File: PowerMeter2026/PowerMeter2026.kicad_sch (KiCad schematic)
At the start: 44 parts, among them J1 STRAIN, J5 USB_C_Receptacle_USB2.0_14P, Q3 MMBT3904, Q4 MMBT3904, SW4 CELL, SW5 RST, SW6 BOOT, U1 ESP32-WROOM-32, U11 HT7733, U5 HX711, U8 LM1117MP-3.3, U9 CH340G, Y2 12MHz

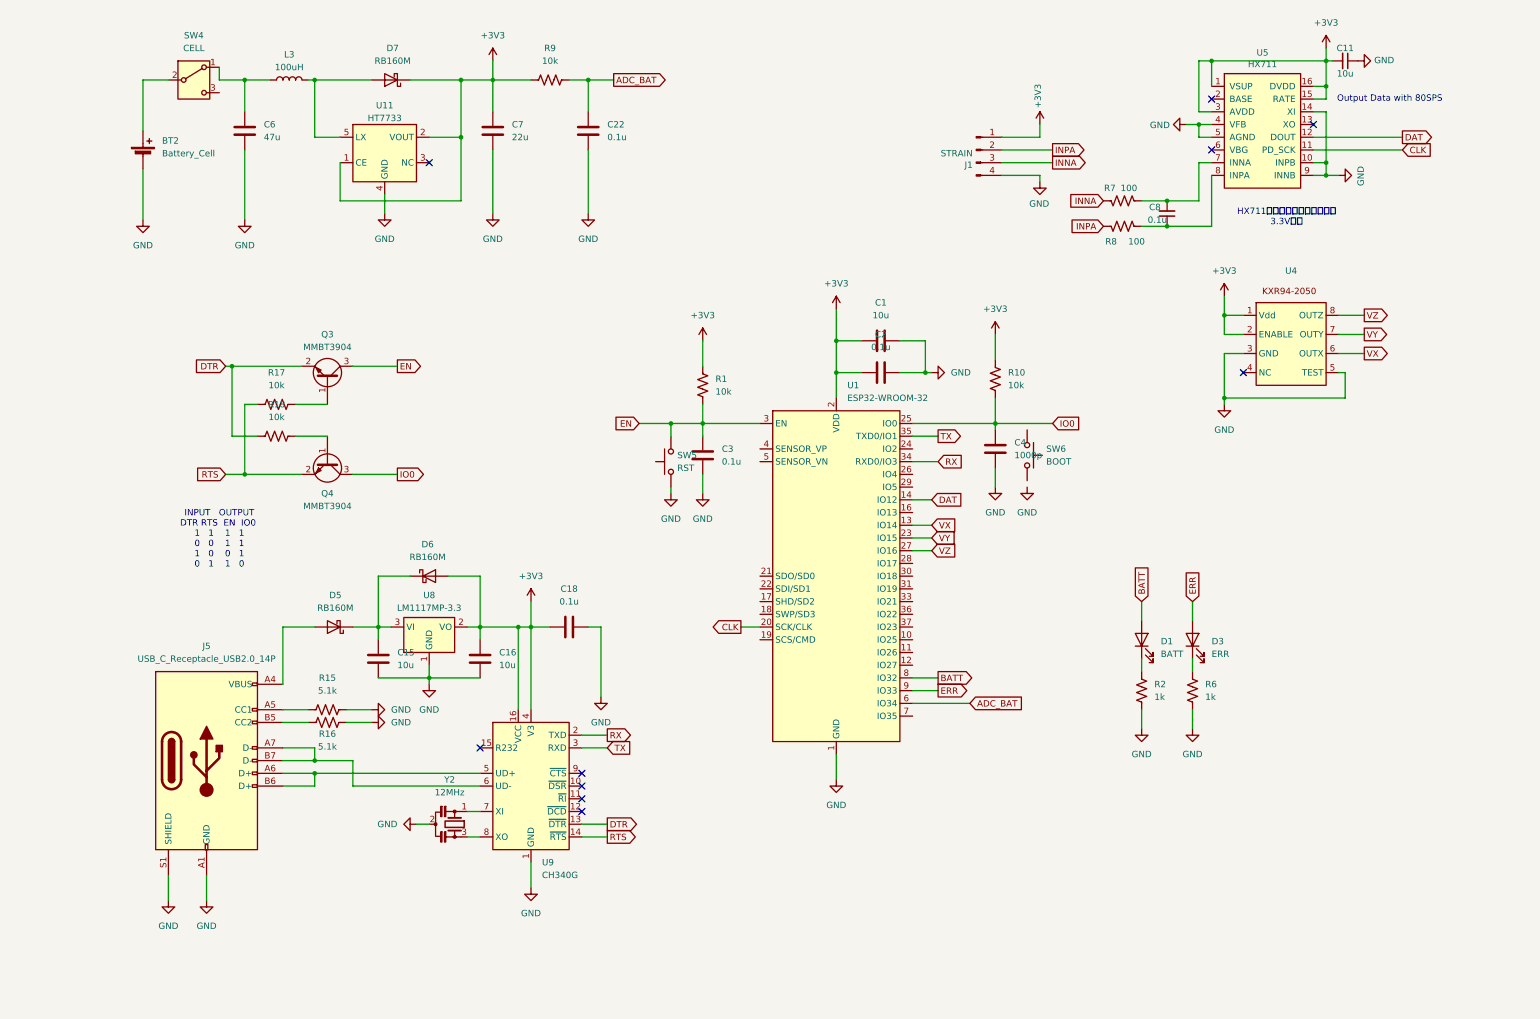
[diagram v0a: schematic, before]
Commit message: Add files via upload
3軸ジャイロからホール素子に変更　2025.09.30
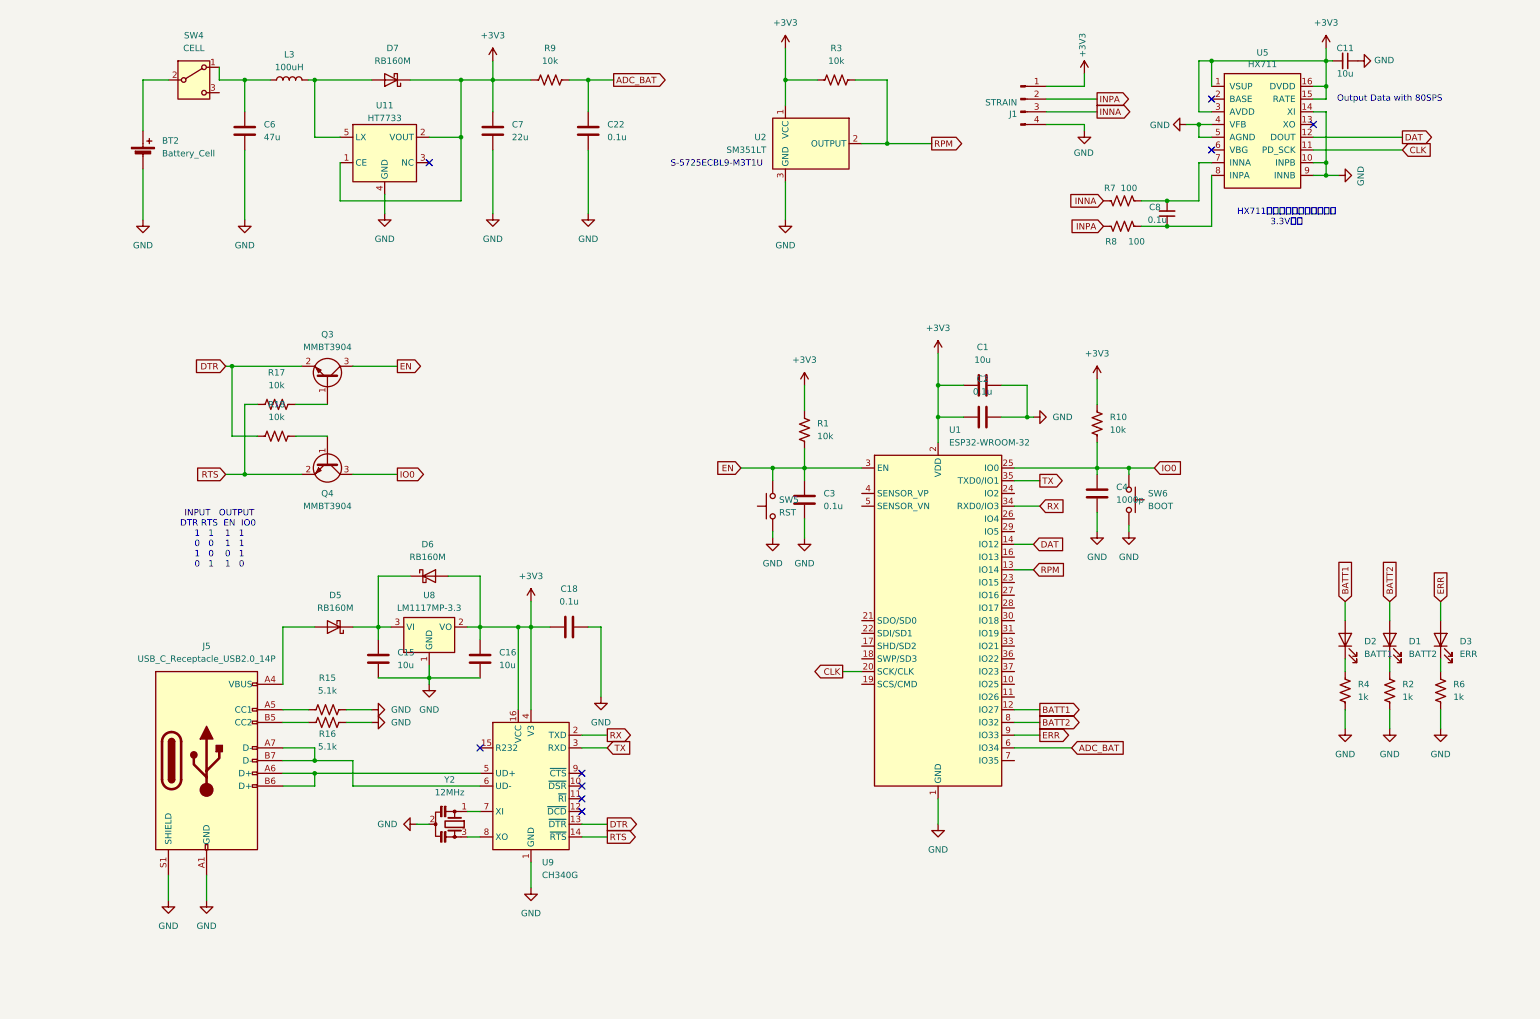
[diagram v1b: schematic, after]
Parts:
- removed U4: ~, Package_DIP:DIP-8_W7.62mm_Socket, symbol KUBTSS_parts:KXR94-2050_mod
- added D2: BATT1, LED_SMD:LED_0603_1608Metric, symbol Device:LED
- added R3: 10k, Resistor_SMD:R_0603_1608Metric, symbol Device:R_US
- added R4: 1k, Resistor_SMD:R_0603_1608Metric, symbol Device:R_US
- added U2: SM351LT, Package_TO_SOT_SMD:SOT-23, symbol Sensor_Magnetic:SM351LT
- D1: value BATT -> BATT2
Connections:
- net +3V3: now also R3.1, U2.1 (VCC)
- net GND: now also SW6.2, R4.2, U2.3 (GND)
- net IO0: now also SW6.1
- net BATT1: now reaches U1.12 (IO27)
- net BATT1: now also D2.2 (A)
- net BATT renamed BATT2
- net VX renamed RPM
- net RPM: now also R3.2, U2.2 (OUTPUT)
- net VY: no longer names the net of U1.23 (IO15)
- net VZ: no longer names the net of U1.27 (IO16)
- new net: D2.1 (K), R4.1
- no-connect marks 10 -> 9
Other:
- note added: "S-5725ECBL9-M3T1U"
- moved on the sheet: C1, C2, C3, C4, D1, D3, J1, R1, R10, R2, R6, SW5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

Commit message: Add files via upload
安定化させた
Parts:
- removed C11: 10u, Capacitor_SMD:C_0603_1608Metric, symbol Device:C_Small
- removed C3: 0.1u, Capacitor_SMD:C_0603_1608Metric, symbol Device:C
- removed C4: 1000p, Capacitor_SMD:C_0603_1608Metric, symbol Device:C
- removed C8: 0.1u, Capacitor_SMD:C_0603_1608Metric, symbol Device:C_Small
- removed D5, D6: RB160M, Diode_SMD:D_SOD-123, symbol Device:D_Schottky
- removed J5: USB_C_Receptacle_USB2.0_14P, Connector_USB:USB_C_Receptacle_HRO_TYPE-C-31-M-12, symbol Connector:USB_C_Receptacle_USB2.0_14P
- removed R10: 10k, Resistor_SMD:R_0603_1608Metric, symbol Device:R_US
- removed SW5: RST, Button_Switch_SMD:SW_SPST_PTS810, symbol Switch:SW_Push
- removed SW6: BOOT, Button_Switch_SMD:SW_SPST_PTS810, symbol Switch:SW_Push
- removed U1: ESP32-WROOM-32, RF_Module:ESP32-WROOM-32, symbol RF_Module:ESP32-WROOM-32
- removed U5: HX711, Package_SO:SOP-16_3.9x9.9mm_P1.27mm, symbol PowerMeter2023-rescue:HX711-RotationBoard_parts
- removed U8: LM1117MP-3.3, Package_TO_SOT_SMD:SOT-223-3_TabPin2, symbol Regulator_Linear:LM1117MP-3.3
- removed U9: CH340G, Package_SO:SOIC-16_3.9x9.9mm_P1.27mm, symbol Interface_USB:CH340G
- removed Y2: 12MHz, Crystal:Resonator_SMD_Murata_CSTxExxV-3Pin_3.0x1.1mm, symbol Device:Resonator_Small
- added C10, C13, C14, C8: 0.1u, Capacitor_SMD:C_0603_1608Metric, symbol Device:C
- added C11, C23: 1u, Capacitor_SMD:C_0603_1608Metric, symbol Device:C
- added C12, C17, C9: 10u, Capacitor_SMD:C_1206_3216Metric, symbol Device:C
- added C19, C4: 0.1u, Capacitor_SMD:C_0603_1608Metric, symbol Device:C_Small
- added C20: 1000p, Capacitor_SMD:C_0603_1608Metric, symbol Device:C
- added C21, C3: 10u, Capacitor_SMD:C_0603_1608Metric, symbol Device:C_Small
- added C24: 1n, Capacitor_SMD:C_0603_1608Metric, symbol Device:C
- added C5: 1n, Capacitor_SMD:C_1206_3216Metric, symbol Device:C
- added D4, D8: RB160M, Diode_SMD:D_SOD-123, symbol Device:D_Schottky
- added F1: Fuse, symbol Device:Fuse
- added J2: USB_C_Receptacle_USB2.0_14P, Connector_USB:USB_C_Receptacle_HRO_TYPE-C-31-M-12, symbol Connector:USB_C_Receptacle_USB2.0_14P
- added Q1: MMBT3906, Package_TO_SOT_SMD:SOT-23, symbol Transistor_BJT:MMBT3906
- added R11, R12: 5.1k, Resistor_SMD:R_0603_1608Metric, symbol Device:R_US
- added R13, R14: 22, Resistor_SMD:R_0603_1608Metric, symbol Device:R_US
- added R19, R20: 0.3, Resistor_SMD:R_0603_1608Metric, symbol Device:R_US
- added R21: 3.3k, Resistor_SMD:R_0603_1608Metric, symbol Device:R_US
- added R22, R24, R30: 100, Resistor_SMD:R_0603_1608Metric, symbol Device:R_US
- added R23: 6.8k, Resistor_SMD:R_0603_1608Metric, symbol Device:R_US
- added R25: 14k, Resistor_SMD:R_0603_1608Metric, symbol Device:R_US
- added R26, R31: 10k, Resistor_SMD:R_0603_1608Metric, symbol Device:R_US
- added R5: 1M, Resistor_SMD:R_0603_1608Metric, symbol Device:R_US
- added SW1: RST, Button_Switch_SMD:SW_SPST_PTS810, symbol Switch:SW_Push
- added SW2: BOOT, Button_Switch_SMD:SW_SPST_PTS810, symbol Switch:SW_Push
- added U3: LM1117MP-3.3, Package_TO_SOT_SMD:SOT-223-3_TabPin2, symbol Regulator_Linear:LM1117MP-3.3
- added U4: CH340G, Package_SO:SOIC-16_3.9x9.9mm_P1.27mm, symbol Interface_USB:CH340G
- added U6: ESP32-WROOM-32, RF_Module:ESP32-WROOM-32, symbol RF_Module:ESP32-WROOM-32
- added U7: HX711, Package_SO:SOP-16_3.9x9.9mm_P1.27mm, symbol PowerMeter2023-rescue:HX711-RotationBoard_parts
- added Y1: 12MHz, Crystal:Resonator_SMD_Murata_CSTxExxV-3Pin_3.0x1.1mm, symbol Device:Resonator_Small
- C1: value 10u -> 0.1u; footprint Capacitor_SMD:C_1206_3216Metric -> Capacitor_SMD:C_0603_1608Metric
- C15: value 10u -> 0.47u; footprint Capacitor_SMD:C_1206_3216Metric -> Capacitor_SMD:C_0603_1608Metric
- C16: value 10u -> 100u
- L3: value 100uH -> 47uH
- R1: value 10k -> 100k
- R15: value 5.1k -> 10k
- R16: value 5.1k -> 100
- R8: value 100 -> 100k
- R9: value 10k -> 1k
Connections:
- net +3V3: now also C1.2, R1.2, R15.1, C12.1, C14.1, C17.1, C23.1, D8.2 (A), R31.1, U3.2 (VO), U6.2 (VDD); no longer C1.1, R1.1, U11.1 (CE), U2.1 (VCC)
- net ADC_BAT: now also U6.31 (IO19)
- net BATT1: now also U6.27 (IO16)
- net BATT2: now also U6.28 (IO17)
- net CLK: now also U7.11 (PD_SCK)
- net DAT: now also U6.16 (IO13), U7.12 (DOUT)
- net DTR: now also U4.13 (~{DTR})
- net EN: now also C15.1, R15.2, SW1.2, U6.3 (EN); no longer R1.2
- net ERR: now also U6.30 (IO18)
- net GND: now also R8.2, C11.2, C13.2, C14.2, C17.2, C20.2, C21.1, C24.2, C3.1, C4.2, C5.2, C8.2, J2.A1 (GND), J2.A12 (GND), J2.B1 (GND), J2.B12 (GND), R11.2, R12.1, R19.2, R20.1, R23.2, R26.2, R5.2, SW1.1, SW2.2, U3.1 (GND), U4.1 (GND), U6.1 (GND), U6.15 (GND), U6.38 (GND), U6.39 (GND), U7.10 (INPB), U7.14 (XI), U7.5 (AGND), U7.9 (INNB), Y1.2; no longer C1.2, C2.2, R15.2, R16.1, U2.3 (GND)
- net INNA: now also R16.1; no longer R7.1
- net INPA: now also R24.1; no longer R8.1
- net IO0: now also C20.1, R30.2, R31.2, SW2.1
- net RPM: now also R7.2, U6.13 (IO14); no longer R3.2, U2.2 (OUTPUT)
- net RTS: now also U4.14 (~{RTS})
- net RX: now also R21.1, R23.1, U6.34 (RXD0/IO3)
- net TX: now also R22.1, U6.35 (TXD0/IO1)
- net at R16.2: now also C19.2, U7.7 (INNA)
- new net: C10.2, U4.16 (VCC)
- new net: R21.2, U4.2 (TXD)
- new net: R22.2, U4.3 (RXD)
- new net: C13.1, U4.4 (V3)
- new net: R13.1, U4.5 (UD+)
- new net: R14.1, U4.6 (UD-)
- new net: U4.7 (XI), Y1.1
- new net: U4.8 (XO), Y1.3
- new net: J2.A5 (CC1), R11.1
- new net: C10.1, C9.1, D4.1 (K), D8.1 (K), U3.3 (VI)
- new net: C9.2, R19.1
- new net: C11.1, C8.1, U2.3 (GND)
- new net: J2.A7 (D-), J2.B7 (D-), R14.2
- new net: R30.1, U6.25 (IO0)
- new net: J2.B5 (CC2), R12.2
- new net: C19.1, R24.2, U7.8 (INPA)
- new net: C5.1, J2.S1 (SHIELD), R5.1
- new net: C1.1, R1.1, U11.1 (CE)
- new net: Q1.1 (B), U7.2 (BASE)
- new net: C2.2, C23.2, U2.1 (VCC)
- new net: C24.1, R3.2, R7.1, U2.2 (OUTPUT)
- new net: D4.2 (A), F1.1
- new net: F1.2, J2.A4 (VBUS), J2.A9 (VBUS), J2.B4 (VBUS), J2.B9 (VBUS)
- new net: J2.A6 (D+), J2.B6 (D+), R13.2
- new net: R25.2, R26.1, U7.4 (VFB)
- new net: C4.1, U7.6 (VBG)
- new net: C12.2, R20.2
- new net: R8.1, U6.14 (IO12)
- new net +5V: C21.2, Q1.2 (E), U7.1 (VSUP), U7.15 (RATE), U7.16 (DVDD)
- new net VDDA: C3.2, Q1.3 (C), R25.1, U7.3 (AVDD)
- no-connect marks 9 -> 7
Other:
- note added: "2~3Aクラスのインダクタを使う"
- note added: "IO12 100kΩプルダウン必須"
- note added: "L3のVinに可能な 限り近づける"
- note added: "Use Internal Oscillator"
- note added: "省電力のため"
- moved on the sheet: BT2, R3, SW4, U2
